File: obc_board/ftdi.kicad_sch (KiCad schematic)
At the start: 20 parts, among them U17 AP2127N-3.3, U18 FT4232H-56Q-REEL, Y2 12MHz

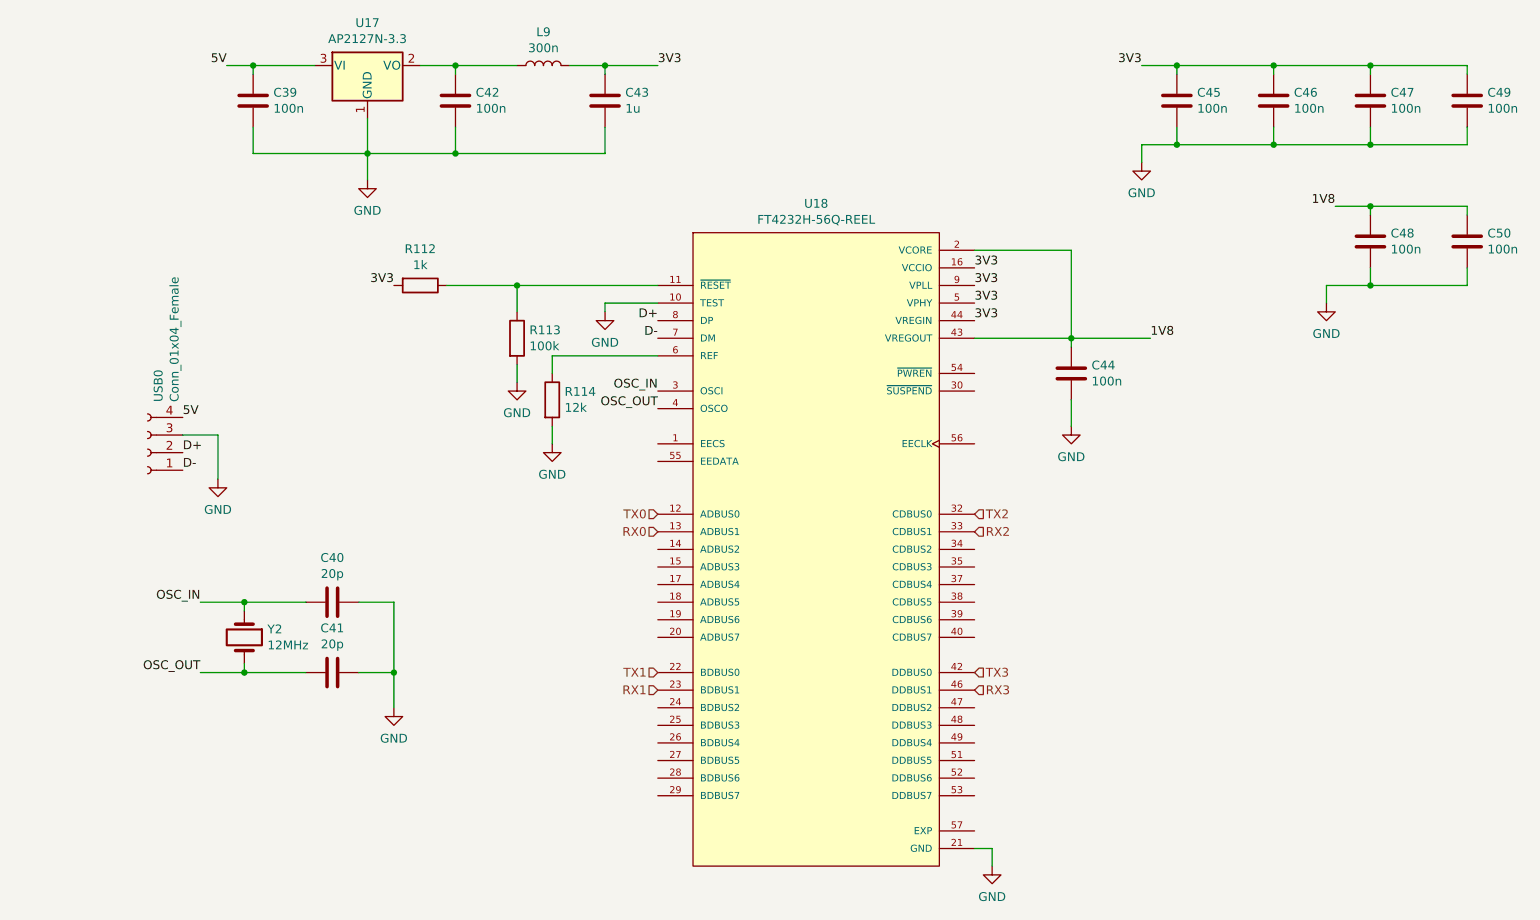
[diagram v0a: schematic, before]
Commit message: changed magnetorquer driver IC and changed power switch IC
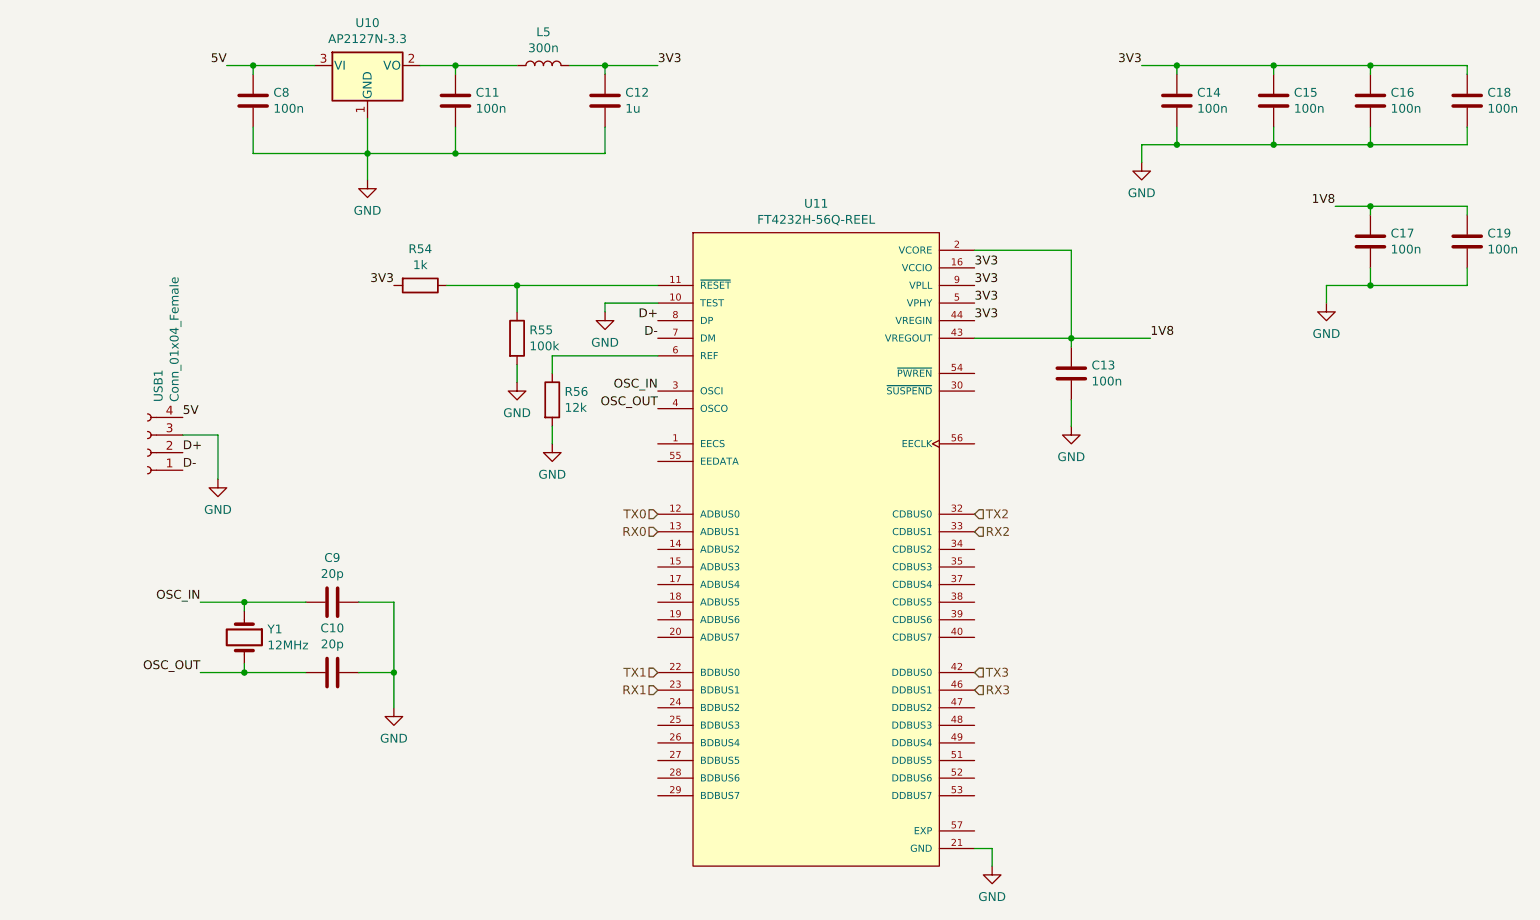
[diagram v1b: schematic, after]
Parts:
- renumbered C41 to C10, C42 to C11, C43 to C12, C44 to C13, C45 to C14, C46 to C15, C47 to C16, C48 to C17, C49 to C18, C50 to C19, C39 to C8, C40 to C9, L9 to L5, R112 to R54, R113 to R55, R114 to R56, U17 to U10, U18 to U11, USB0 to USB1, Y2 to Y1
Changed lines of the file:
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@@
   (symbol (lib_id "cubesat_obc_lib:FT4232H-56Q-REEL") (at 165.1 116.84 0) (unit 1)
     (in_bom yes) (on_board yes)
-    (property "Reference" "U18" (id 0) (at 165.1 61.849 0))
+    (property "Reference" "U11" (id 0) (at 165.1 61.849 0))
     (property "Value" "FT4232H-56Q-REEL" (id 1) (at 165.1 64.1604 0))
     (property "Footprint" "QFN50P800X800X100-57N" (id 2) (at 165.1 116.84 0)
@@
   (symbol (lib_id "Device:R") (at 107.95 73.66 270) (unit 1)
     (in_bom yes) (on_board yes)
-    (property "Reference" "R112" (id 0) (at 107.95 68.4022 90))
+    (property "Reference" "R54" (id 0) (at 107.95 68.4022 90))
     (property "Value" "1k" (id 1) (at 107.95 70.7136 90))
     (property "Footprint" "Resistor_SMD:R_0402_1005Metric" (id 2) (at 107.95 71.882 90)
@@
   (symbol (lib_id "Device:R") (at 121.92 81.28 0) (unit 1)
     (in_bom yes) (on_board yes)
-    (property "Reference" "R113" (id 0) (at 123.698 80.1116 0)
+    (property "Reference" "R55" (id 0) (at 123.698 80.1116 0)
       (effects (font (size 1.27 1.27)) (justify left))
     )
@@
   (symbol (lib_id "Device:R") (at 127 90.17 0) (unit 1)
     (in_bom yes) (on_board yes)
-    (property "Reference" "R114" (id 0) (at 128.778 89.0016 0)
+    (property "Reference" "R56" (id 0) (at 128.778 89.0016 0)
       (effects (font (size 1.27 1.27)) (justify left))
     )
@@
   (symbol (lib_id "Connector:Conn_01x04_Female") (at 68.58 97.79 180) (unit 1)
     (in_bom yes) (on_board yes)
-    (property "Reference" "USB0" (id 0) (at 70.1548 90.4748 90)
+    (property "Reference" "USB1" (id 0) (at 70.1548 90.4748 90)
       (effects (font (size 1.27 1.27)) (justify right))
     )
@@
   (symbol (lib_id "Regulator_Linear:AP2127N-3.3") (at 100.33 41.91 0) (unit 1)
     (in_bom yes) (on_board yes)
-    (property "Reference" "U17" (id 0) (at 100.33 35.7632 0))
+    (property "Reference" "U10" (id 0) (at 100.33 35.7632 0))
     (property "Value" "AP2127N-3.3" (id 1) (at 100.33 38.0746 0))
     (property "Footprint" "Package_TO_SOT_SMD:SOT-23" (id 2) (at 100.33 36.195 0)
@@
   (symbol (lib_id "Device:C") (at 83.82 46.99 0) (unit 1)
     (in_bom yes) (on_board yes)
-    (property "Reference" "C39" (id 0) (at 86.741 45.8216 0)
+    (property "Reference" "C8" (id 0) (at 86.741 45.8216 0)
       (effects (font (size 1.27 1.27)) (justify left))
     )
@@
   (symbol (lib_id "Device:C") (at 113.03 46.99 0) (unit 1)
     (in_bom yes) (on_board yes)
-    (property "Reference" "C42" (id 0) (at 115.951 45.8216 0)
+    (property "Reference" "C11" (id 0) (at 115.951 45.8216 0)
       (effects (font (size 1.27 1.27)) (justify left))
     )
@@
   (symbol (lib_id "Device:C") (at 201.93 86.36 0) (unit 1)
     (in_bom yes) (on_board yes)
-    (property "Reference" "C44" (id 0) (at 204.851 85.1916 0)
+    (property "Reference" "C13" (id 0) (at 204.851 85.1916 0)
       (effects (font (size 1.27 1.27)) (justify left))
     )
@@
   (symbol (lib_id "Device:C") (at 217.17 46.99 0) (unit 1)
     (in_bom yes) (on_board yes)
-    (property "Reference" "C45" (id 0) (at 220.091 45.8216 0)
+    (property "Reference" "C14" (id 0) (at 220.091 45.8216 0)
       (effects (font (size 1.27 1.27)) (justify left))
     )
@@
   (symbol (lib_id "Device:C") (at 231.14 46.99 0) (unit 1)
     (in_bom yes) (on_board yes)
-    (property "Reference" "C46" (id 0) (at 234.061 45.8216 0)
+    (property "Reference" "C15" (id 0) (at 234.061 45.8216 0)
       (effects (font (size 1.27 1.27)) (justify left))
     )
@@
   (symbol (lib_id "Device:C") (at 245.11 46.99 0) (unit 1)
     (in_bom yes) (on_board yes)
-    (property "Reference" "C47" (id 0) (at 248.031 45.8216 0)
+    (property "Reference" "C16" (id 0) (at 248.031 45.8216 0)
       (effects (font (size 1.27 1.27)) (justify left))
     )
@@
   (symbol (lib_id "Device:C") (at 259.08 46.99 0) (unit 1)
     (in_bom yes) (on_board yes)
-    (property "Reference" "C49" (id 0) (at 262.001 45.8216 0)
+    (property "Reference" "C18" (id 0) (at 262.001 45.8216 0)
       (effects (font (size 1.27 1.27)) (justify left))
     )
@@
   (symbol (lib_id "Device:C") (at 245.11 67.31 0) (unit 1)
     (in_bom yes) (on_board yes)
-    (property "Reference" "C48" (id 0) (at 248.031 66.1416 0)
+    (property "Reference" "C17" (id 0) (at 248.031 66.1416 0)
       (effects (font (size 1.27 1.27)) (justify left))
     )
@@
   (symbol (lib_id "Device:C") (at 259.08 67.31 0) (unit 1)
     (in_bom yes) (on_board yes)
-    (property "Reference" "C50" (id 0) (at 262.001 66.1416 0)
+    (property "Reference" "C19" (id 0) (at 262.001 66.1416 0)
       (effects (font (size 1.27 1.27)) (justify left))
     )
@@
   (symbol (lib_id "Device:L") (at 125.73 41.91 90) (unit 1)
     (in_bom yes) (on_board yes)
-    (property "Reference" "L9" (id 0) (at 125.73 37.084 90))
+    (property "Reference" "L5" (id 0) (at 125.73 37.084 90))
     (property "Value" "300n" (id 1) (at 125.73 39.3954 90))
     (property "Footprint" "Inductor_SMD:L_1210_3225Metric" (id 2) (at 125.73 41.91 0)
@@
   (symbol (lib_id "Device:C") (at 134.62 46.99 0) (unit 1)
     (in_bom yes) (on_board yes)
-    (property "Reference" "C43" (id 0) (at 137.541 45.8216 0)
+    (property "Reference" "C12" (id 0) (at 137.541 45.8216 0)
       (effects (font (size 1.27 1.27)) (justify left))
     )
@@
   (symbol (lib_id "Device:Crystal") (at 82.55 124.46 270) (unit 1)
     (in_bom yes) (on_board yes)
-    (property "Reference" "Y2" (id 0) (at 85.8774 123.2916 90)
+    (property "Reference" "Y1" (id 0) (at 85.8774 123.2916 90)
       (effects (font (size 1.27 1.27)) (justify left))
     )
@@
   (symbol (lib_id "Device:C") (at 95.25 119.38 270) (mirror x) (unit 1)
     (in_bom yes) (on_board yes)
-    (property "Reference" "C40" (id 0) (at 95.25 112.9792 90))
+    (property "Reference" "C9" (id 0) (at 95.25 112.9792 90))
     (property "Value" "20p" (id 1) (at 95.25 115.2906 90))
     (property "Footprint" "Capacitor_SMD:C_0201_0603Metric" (id 2) (at 91.44 118.4148 0)
@@
   (symbol (lib_id "Device:C") (at 95.25 129.54 270) (unit 1)
     (in_bom yes) (on_board yes)
-    (property "Reference" "C41" (id 0) (at 95.25 123.1392 90))
+    (property "Reference" "C10" (id 0) (at 95.25 123.1392 90))
     (property "Value" "20p" (id 1) (at 95.25 125.4506 90))
     (property "Footprint" "Capacitor_SMD:C_0201_0603Metric" (id 2) (at 91.44 130.5052 0)
@@
   (symbol (lib_id "power:GND") (at 201.93 93.98 0) (unit 1)
     (in_bom yes) (on_board yes) (fields_autoplaced)
-    (property "Reference" "#PWR?" (id 0) (at 201.93 100.33 0)
+    (property "Reference" "#PWR031" (id 0) (at 201.93 100.33 0)
       (effects (font (size 1.27 1.27)) hide)
     )
@@
   (symbol (lib_id "power:GND") (at 121.92 87.63 0) (unit 1)
     (in_bom yes) (on_board yes) (fields_autoplaced)
-    (property "Reference" "#PWR?" (id 0) (at 121.92 93.98 0)
+    (property "Reference" "#PWR027" (id 0) (at 121.92 93.98 0)
       (effects (font (size 1.27 1.27)) hide)
     )
@@
   (symbol (lib_id "power:GND") (at 104.14 134.62 0) (unit 1)
     (in_bom yes) (on_board yes) (fields_autoplaced)
-    (property "Reference" "#PWR?" (id 0) (at 104.14 140.97 0)
+    (property "Reference" "#PWR026" (id 0) (at 104.14 140.97 0)
       (effects (font (size 1.27 1.27)) hide)
     )
@@
   (symbol (lib_id "power:GND") (at 100.33 58.42 0) (unit 1)
     (in_bom yes) (on_board yes) (fields_autoplaced)
-    (property "Reference" "#PWR?" (id 0) (at 100.33 64.77 0)
+    (property "Reference" "#PWR025" (id 0) (at 100.33 64.77 0)
       (effects (font (size 1.27 1.27)) hide)
     )
@@
   (symbol (lib_id "power:GND") (at 238.76 76.2 0) (unit 1)
     (in_bom yes) (on_board yes) (fields_autoplaced)
-    (property "Reference" "#PWR?" (id 0) (at 238.76 82.55 0)
+    (property "Reference" "#PWR033" (id 0) (at 238.76 82.55 0)
       (effects (font (size 1.27 1.27)) hide)
     )
@@
   (symbol (lib_id "power:GND") (at 78.74 101.6 0) (unit 1)
     (in_bom yes) (on_board yes) (fields_autoplaced)
-    (property "Reference" "#PWR?" (id 0) (at 78.74 107.95 0)
+    (property "Reference" "#PWR024" (id 0) (at 78.74 107.95 0)
       (effects (font (size 1.27 1.27)) hide)
     )
@@
   (symbol (lib_id "power:GND") (at 190.5 157.48 0) (unit 1)
     (in_bom yes) (on_board yes) (fields_autoplaced)
-    (property "Reference" "#PWR?" (id 0) (at 190.5 163.83 0)
+    (property "Reference" "#PWR030" (id 0) (at 190.5 163.83 0)
       (effects (font (size 1.27 1.27)) hide)
     )
@@
   (symbol (lib_id "power:GND") (at 134.62 77.47 0) (unit 1)
     (in_bom yes) (on_board yes) (fields_autoplaced)
-    (property "Reference" "#PWR?" (id 0) (at 134.62 83.82 0)
+    (property "Reference" "#PWR029" (id 0) (at 134.62 83.82 0)
       (effects (font (size 1.27 1.27)) hide)
     )
@@
   (symbol (lib_id "power:GND") (at 127 96.52 0) (unit 1)
     (in_bom yes) (on_board yes) (fields_autoplaced)
-    (property "Reference" "#PWR?" (id 0) (at 127 102.87 0)
+    (property "Reference" "#PWR028" (id 0) (at 127 102.87 0)
       (effects (font (size 1.27 1.27)) hide)
     )
@@
   (symbol (lib_id "power:GND") (at 212.09 55.88 0) (unit 1)
     (in_bom yes) (on_board yes) (fields_autoplaced)
-    (property "Reference" "#PWR?" (id 0) (at 212.09 62.23 0)
-      (effects (font (size 1.27 1.27)) hide)
-    )
+    (property "Reference" "#PWR032" (id 0) (at 212.09 62.23 0)
+      (effects (font (size 1.27 1.27)) hide)
+    )

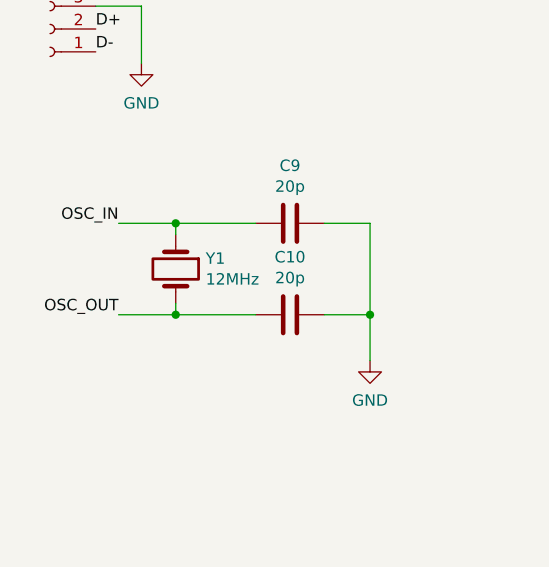
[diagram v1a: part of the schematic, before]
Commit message: updated digikey part numbers and footprints
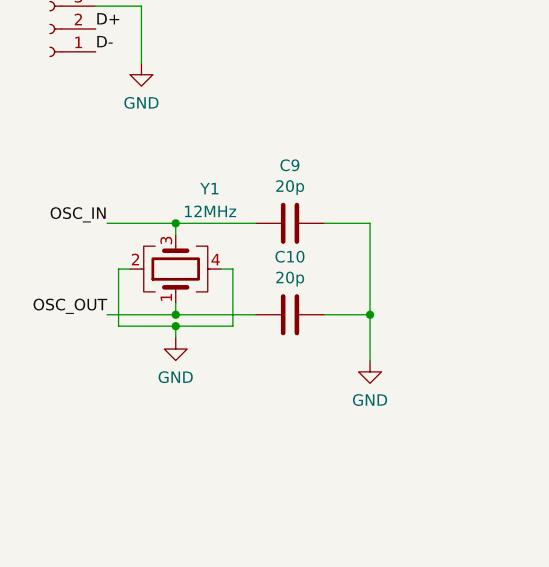
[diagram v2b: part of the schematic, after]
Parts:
- removed Y1: 12MHz, Crystal:Crystal_SMD_5032-4Pin_5.0x3.2mm, symbol Device:Crystal
- added Y1: 12MHz, Crystal:Crystal_SMD_5032-4Pin_5.0x3.2mm, symbol Device:Crystal_GND24
- C10, C9: footprint Capacitor_SMD:C_0201_0603Metric -> Capacitor_SMD:C_0603_1608Metric; Digikey Part Number 490-9618-1-ND -> 399-C0603C200K4HACAUTOCT-ND
- C11, C13, C14, C15, C16, C17, C18, C19, C8: Digikey Part Number 490-16433-1-ND -> 399-6828-1-ND
- C12: Digikey Part Number 311-1446-2-ND -> 399-17713-1-ND
- L5: footprint Inductor_SMD:L_1210_3225Metric -> Inductor_SMD:L_Taiyo-Yuden_MD-3030; Digikey Part Number 732-7338-2-ND -> 587-5612-1-ND
- R54: Digikey Part Number 311-1.00KLRCT-ND -> 311-1KLBCT-ND
- R55: Digikey Part Number YAG2307CT-ND -> YAG3434CT-ND
- R56: Digikey Part Number 541-12.0KAABTR-ND -> YAG5153CT-ND
- U11: Digikey Part Number 768-1378-1-ND -> (none)
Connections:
- net GND: now also Y1.2, Y1.4
- net OSC_IN: now also Y1.3
- net OSC_OUT: now also Y1.1

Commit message: updated pcb
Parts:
- U11: footprint QFN50P800X800X100-57N -> Package_DFN_QFN:QFN-56-1EP_8x8mm_P0.5mm_EP5.9x5.9mm
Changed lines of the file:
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@@
     (property "Reference" "U11" (id 0) (at 165.1 61.849 0))
     (property "Value" "FT4232H-56Q-REEL" (id 1) (at 165.1 64.1604 0))
-    (property "Footprint" "QFN50P800X800X100-57N" (id 2) (at 165.1 116.84 0)
+    (property "Footprint" "Package_DFN_QFN:QFN-56-1EP_8x8mm_P0.5mm_EP5.9x5.9mm" (id 2) (at 165.1 116.84 0)
       (effects (font (size 1.27 1.27)) (justify left bottom) hide)
     )

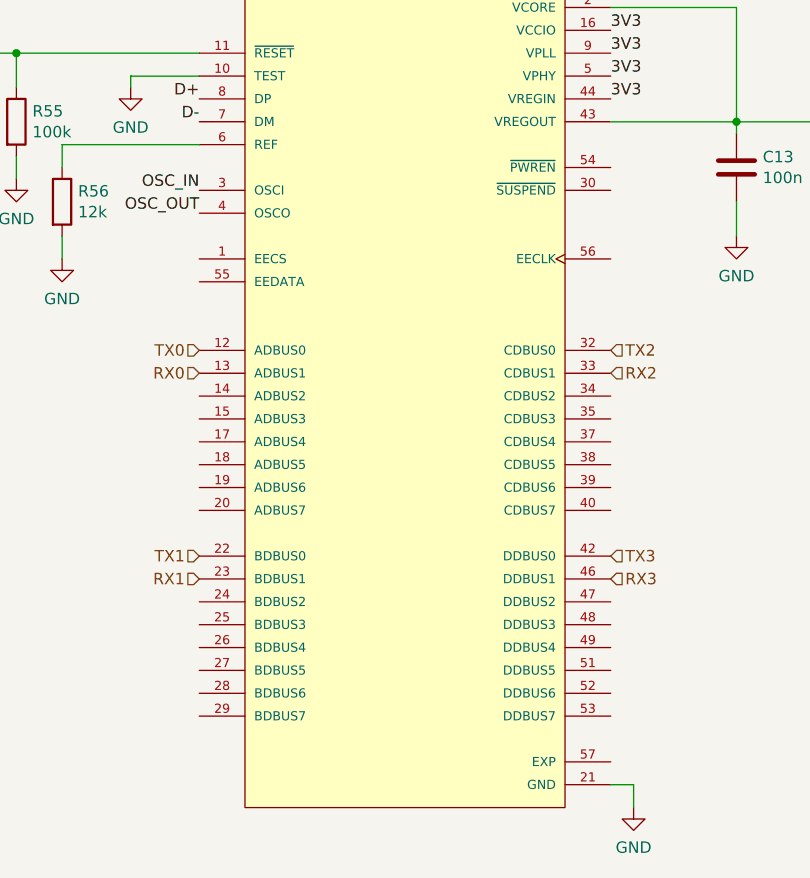
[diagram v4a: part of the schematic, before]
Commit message: added silkscreen labels and gerber file
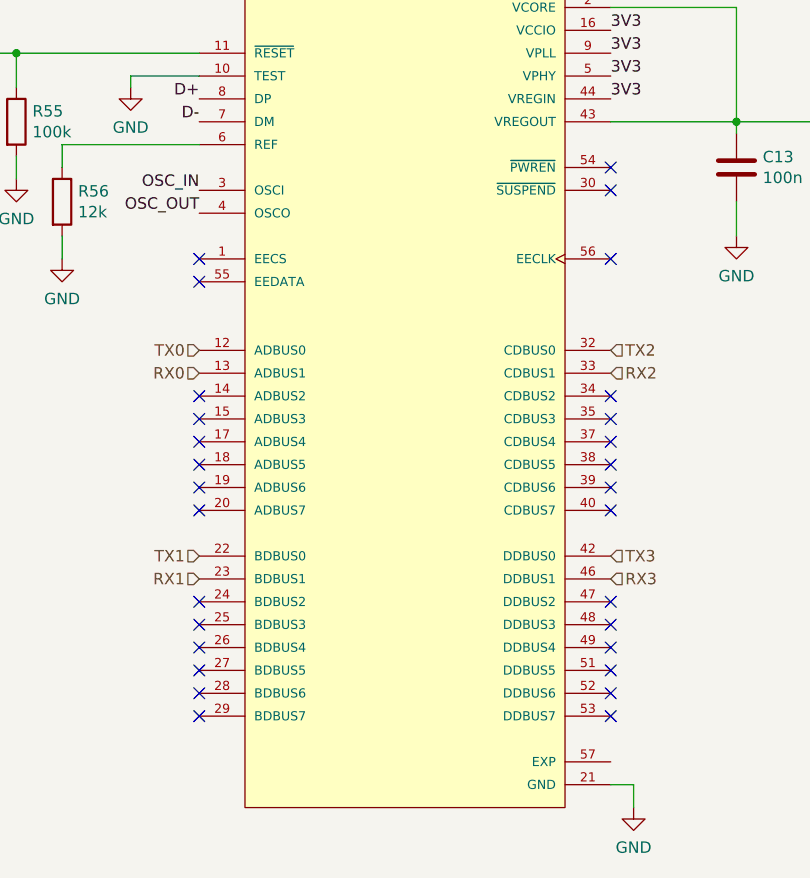
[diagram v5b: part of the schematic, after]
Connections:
- no-connect marks 0 -> 29
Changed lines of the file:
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@@
   (junction (at 245.11 62.23) (diameter 0) (color 0 0 0 0)
   )
+  (no_connect (at 142.24 121.92))
+  (no_connect (at 142.24 124.46))
+  (no_connect (at 142.24 99.06))
+  (no_connect (at 142.24 96.52))
+  (no_connect (at 142.24 119.38))
+  (no_connect (at 142.24 116.84))
+  (no_connect (at 187.96 96.52))
+  (no_connect (at 187.96 86.36))
+  (no_connect (at 187.96 88.9))
+  (no_connect (at 142.24 134.62))
+  (no_connect (at 142.24 137.16))
+  (no_connect (at 142.24 139.7))
+  (no_connect (at 142.24 111.76))
+  (no_connect (at 142.24 114.3))
+  (no_connect (at 187.96 124.46))
+  (no_connect (at 187.96 119.38))
+  (no_connect (at 187.96 121.92))
+  (no_connect (at 187.96 147.32))
+  (no_connect (at 142.24 142.24))
+  (no_connect (at 142.24 144.78))
+  (no_connect (at 142.24 147.32))
+  (no_connect (at 187.96 134.62))
+  (no_connect (at 187.96 137.16))
+  (no_connect (at 187.96 139.7))
+  (no_connect (at 187.96 142.24))
+  (no_connect (at 187.96 144.78))
+  (no_connect (at 187.96 111.76))
+  (no_connect (at 187.96 114.3))
+  (no_connect (at 187.96 116.84))
   (wire (pts (xy 100.33 49.53) (xy 100.33 54.61))
     (stroke (width 0) (type default) (color 0 0 0 0))
